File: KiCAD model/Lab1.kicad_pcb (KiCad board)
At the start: 2 copper layers, 60 x 40 mm, 47 parts, among them J1 USB_OTG, J2 SWD, SW2 Reset, U1 PMW3389, U2 AP2125N-3.3TRG, U3 MIC5235YM5-TR, U4 STM32F411RETx, U5 USBLC6-2SC6, Y1 16Mhz

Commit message: orgot the model
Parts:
- removed SW2: Reset, Button_Switch_SMD:SW_SPST_B3U-1000P
- added C22: 100n, Capacitor_SMD:C_0805_2012Metric_Pad1.18x1.45mm_HandSolder, F.Cu at (150.7, 85.9)
- added C23: 100n, Capacitor_SMD:C_0805_2012Metric_Pad1.18x1.45mm_HandSolder, F.Cu at (169.9, 67.1)
- added C24: 100n, Capacitor_SMD:C_0805_2012Metric_Pad1.18x1.45mm_HandSolder, F.Cu at (165.9, 71.7)
- added C25: 100n, Capacitor_SMD:C_0805_2012Metric_Pad1.18x1.45mm_HandSolder, F.Cu at (185.6, 52.3)
- added C26: 100n, Capacitor_SMD:C_0805_2012Metric_Pad1.18x1.45mm_HandSolder, F.Cu at (191.2, 48.9)
- added C27: 100n, Capacitor_SMD:C_0805_2012Metric_Pad1.18x1.45mm_HandSolder, F.Cu at (150.7, 88.9)
- added C28: 100n, Capacitor_SMD:C_0805_2012Metric_Pad1.18x1.45mm_HandSolder, F.Cu at (155.6, 84.2)
- added C30: 10u, Capacitor_SMD:C_0805_2012Metric_Pad1.18x1.45mm_HandSolder, F.Cu at (170.9, 73.2)
- added C31: 100n, Capacitor_SMD:C_0805_2012Metric_Pad1.18x1.45mm_HandSolder, F.Cu at (181.7, 60.1)
- added C32: 4.7u, Capacitor_SMD:C_0805_2012Metric_Pad1.18x1.45mm_HandSolder, F.Cu at (179.5, 66.4)
- added C33: 100n, Capacitor_SMD:C_0805_2012Metric_Pad1.18x1.45mm_HandSolder, F.Cu at (191.3, 55.3)
- added C34: 100n, Capacitor_SMD:C_0805_2012Metric_Pad1.18x1.45mm_HandSolder, F.Cu at (175.5, 70.2)
- added D4: Indicator LED, LED_SMD:LED_1206_3216Metric, F.Cu at (160.7, 71.8)
- added D5: Indicator LED, LED_SMD:LED_1206_3216Metric, F.Cu at (145.5, 86.1)
- added D6: Indicator LED, LED_SMD:LED_1206_3216Metric, F.Cu at (170.3, 63.9)
- added JP2: DFU, Connector:FanPinHeader_1x03_P2.54mm_Vertical, F.Cu at (185.4, 43.1)
- added JP3: DFU, Connector:FanPinHeader_1x03_P2.54mm_Vertical, F.Cu at (145.8, 80.0)
- added JP4: DFU, Connector:FanPinHeader_1x03_P2.54mm_Vertical, F.Cu at (171.9, 57.5)
- added R10: 10k, Resistor_SMD:R_0805_2012Metric_Pad1.20x1.40mm_HandSolder, F.Cu at (175.6, 76.1)
- added R11: 150, Resistor_SMD:R_0805_2012Metric_Pad1.20x1.40mm_HandSolder, F.Cu at (180.3, 69.3)
- added R12: 150, Resistor_SMD:R_0805_2012Metric_Pad1.20x1.40mm_HandSolder, F.Cu at (196.1, 53.4)
- added R13: 10k, Resistor_SMD:R_0805_2012Metric_Pad1.20x1.40mm_HandSolder, F.Cu at (170.9, 79.1)
- added R14: 10k, Resistor_SMD:R_0805_2012Metric_Pad1.20x1.40mm_HandSolder, F.Cu at (191.2, 64.2)
- added R15: 150, Resistor_SMD:R_0805_2012Metric_Pad1.20x1.40mm_HandSolder, F.Cu at (175.7, 73.1)
- added R16: 150, Resistor_SMD:R_0805_2012Metric_Pad1.20x1.40mm_HandSolder, F.Cu at (191.3, 58.3)
- added R17: 10k, Resistor_SMD:R_0805_2012Metric_Pad1.20x1.40mm_HandSolder, F.Cu at (205.6, 44.0)
- added R18: 10k, Resistor_SMD:R_0805_2012Metric_Pad1.20x1.40mm_HandSolder, F.Cu at (186.5, 64.2)
- added R19: 10k, Resistor_SMD:R_0805_2012Metric_Pad1.20x1.40mm_HandSolder, F.Cu at (200.8, 49.9)
- added R20: 10k, Resistor_SMD:R_0805_2012Metric_Pad1.20x1.40mm_HandSolder, F.Cu at (205.5, 47.0)
- added R21: 150, Resistor_SMD:R_0805_2012Metric_Pad1.20x1.40mm_HandSolder, F.Cu at (196.1, 59.3)
- added R22: 10k, Resistor_SMD:R_0805_2012Metric_Pad1.20x1.40mm_HandSolder, F.Cu at (200.9, 52.9)
- added R24: 820, Resistor_SMD:R_0805_2012Metric_Pad1.20x1.40mm_HandSolder, F.Cu at (180.4, 72.3)
- added R25: 820, Resistor_SMD:R_0805_2012Metric_Pad1.20x1.40mm_HandSolder, F.Cu at (185.0, 67.2)
- added R26: 820, Resistor_SMD:R_0805_2012Metric_Pad1.20x1.40mm_HandSolder, F.Cu at (170.0, 84.0)
- added R27: 47, Resistor_SMD:R_0805_2012Metric_Pad1.20x1.40mm_HandSolder, F.Cu at (191.2, 61.3)
- added R28: 10k, Resistor_SMD:R_0805_2012Metric_Pad1.20x1.40mm_HandSolder, F.Cu at (196.1, 56.3)
- added R7: 150, Resistor_SMD:R_0805_2012Metric_Pad1.20x1.40mm_HandSolder, F.Cu at (165.3, 84.0)
- added R8: 150, Resistor_SMD:R_0805_2012Metric_Pad1.20x1.40mm_HandSolder, F.Cu at (126.6, 89.0)
- added R9: 10k, Resistor_SMD:R_0805_2012Metric_Pad1.20x1.40mm_HandSolder, F.Cu at (165.0, 87.1)
- added S1: D2F-FL, Desktop:SW_D2F-FL, F.Cu at (37.0, 34.0)
- added S2: D2F-FL, Desktop:SW_D2F-FL, F.Cu at (72.9, 34.0)
- added S3: D2F-FL, Desktop:SW_D2F-FL, F.Cu at (62.0, 57.0)
- added S4: D2F-FL, Desktop:SW_D2F-FL, F.Cu at (48.0, 57.0)
- added S5: D2F-FL, Desktop:SW_D2F-FL, F.Cu at (34.3, 64.9)
- added S6: D2F-FL, Desktop:SW_D2F-FL, F.Cu at (34.3, 79.0)
- added S7: D2F-FL, Desktop:SW_D2F-FL, F.Cu at (71.0, 46.0)
- added SW1: 1825910-6, Desktop:SW_1825910-6-4, F.Cu at (125.0, 39.0)
- added SW10: Rotary_Encoder, Custom:PEC12R-2120F-N0012, F.Cu at (39.0, 57.0)
- added TP10: TestPoint, TestPoint:TestPoint_Pad_1.5x1.5mm, F.Cu at (179.8, 79.9)
- added TP11: TestPoint, TestPoint:TestPoint_Pad_1.5x1.5mm, F.Cu at (200.2, 59.7)
- added TP12: TestPoint, TestPoint:TestPoint_Pad_1.5x1.5mm, F.Cu at (172.7, 87.3)
- added TP13: TestPoint, TestPoint:TestPoint_Pad_1.5x1.5mm, F.Cu at (188.1, 71.0)
- added TP14: Scroll_b, TestPoint:TestPoint_Pad_1.5x1.5mm, F.Cu at (192.7, 67.5)
- added TP16: wheel_click, TestPoint:TestPoint_Pad_1.5x1.5mm, F.Cu at (183.3, 77.5)
- added TP17: in_D+, TestPoint:TestPoint_Pad_1.5x1.5mm, F.Cu at (203.8, 57.3)
- added TP18: Motion, TestPoint:TestPoint_Pad_1.5x1.5mm, F.Cu at (177.7, 83.5)
- added TP19: VDD, TestPoint:TestPoint_Pad_1.5x1.5mm, F.Cu at (184.6, 70.4)
- added TP20: NCS, TestPoint:TestPoint_Pad_1.5x1.5mm, F.Cu at (188.1, 74.6)
- added TP21: GND, TestPoint:TestPoint_Pad_1.5x1.5mm, F.Cu at (198.9, 63.2)
- added TP22: out_D-, TestPoint:TestPoint_Pad_1.5x1.5mm, F.Cu at (191.7, 71.0)
- added TP23: out_D+, TestPoint:TestPoint_Pad_1.5x1.5mm, F.Cu at (176.3, 87.0)
- added TP24: MISO, TestPoint:TestPoint_Pad_1.5x1.5mm, F.Cu at (196.3, 66.8)
- added TP25: GRD, TestPoint:TestPoint_Pad_1.5x1.5mm, F.Cu at (183.3, 81.1)
- added TP26: MCO1, TestPoint:TestPoint_Pad_1.5x1.5mm, F.Cu at (203.8, 60.9)
- added TP27: MCO2, TestPoint:TestPoint_Pad_1.5x1.5mm, F.Cu at (207.4, 57.3)
- added TP28: GND, TestPoint:TestPoint_Pad_1.5x1.5mm, F.Cu at (191.7, 74.6)
- added TP29: Scroll_a, TestPoint:TestPoint_Pad_1.5x1.5mm, F.Cu at (195.2, 71.0)
- added TP30: BOOT0, TestPoint:TestPoint_Pad_1.5x1.5mm, F.Cu at (186.9, 78.1)
- added TP5: TestPoint, TestPoint:TestPoint_Pad_1.5x1.5mm, F.Cu at (195.4, 62.5)
- added TP9: TestPoint, TestPoint:TestPoint_Pad_1.5x1.5mm, F.Cu at (205.0, 53.8)
- R1: value 1.5k -> 47; footprint Resistor_SMD:R_0815_2038Metric_Pad1.20x4.05mm_HandSolder -> Resistor_SMD:R_0805_2012Metric_Pad1.20x1.40mm_HandSolder
- R2, R3, R4, R5: footprint Resistor_SMD:R_0815_2038Metric_Pad1.20x4.05mm_HandSolder -> Resistor_SMD:R_0805_2012Metric_Pad1.20x1.40mm_HandSolder
- R6: value 47 -> 1.5k; footprint Resistor_SMD:R_0815_2038Metric_Pad1.20x4.05mm_HandSolder -> Resistor_SMD:R_0805_2012Metric_Pad1.20x1.40mm_HandSolder
- TP1: value TestPoint -> 5V
- TP2: value 1.9V -> MOSI
- TP3: value TestPoint -> SCK
- TP6: value TestPoint -> 3.3V
- TP7: value TestPoint -> NRST
- TP8: value TestPoint -> in_D-
- U1: footprint Battery:PMW3389 -> Custom:PMW3389
- moved C3 147.4 mm to (205.7, 41.0), turned to 0 degrees
- moved C4 147.2 mm to (200.9, 44.0)
- moved TP2 146.1 mm to (200.3, 56.1)
- moved C20 132.2 mm to (195.2, 44.4), turned to 0 degrees
- moved R6 131.7 mm to (186.5, 61.3), turned to 0 degrees
- moved TP6 131.5 mm to (205.0, 50.2)
- moved U3 130.7 mm to (181.7, 56.3), turned to 0 degrees
- moved C18 130.6 mm to (200.9, 41.0)
- moved R5 130.4 mm to (200.8, 47.0), turned to 0 degrees
- moved C2 129.5 mm to (196.0, 50.4), turned to 0 degrees
- moved D3 127.5 mm to (186.0, 49.1)
- moved R1 127.1 mm to (175.6, 79.1), turned to 0 degrees
- moved D2 126.7 mm to (195.6, 41.2)
- moved R3 124.2 mm to (170.9, 76.1), turned to 0 degrees
- moved C16 120.2 mm to (174.7, 67.1)
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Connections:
- R1 pad 1: Net-(D1-Pad2) -> Net-(JP2-Pad1)
- R1 pad 2: +5V -> Net-(D3-Pad2)
- R5 pad 1: Net-(D2-Pad2) -> Net-(JP3-Pad1)
- R5 pad 2: +3V3 -> Net-(D2-Pad2)
- R6 pad 1: Net-(D3-Pad2) -> Net-(JP4-Pad1)
- R6 pad 2: VDD -> Net-(D1-Pad2)
- TP1 pad 1: +3V3 -> +5V
- TP2 pad 1: VDD -> MOSI
- TP3 pad 1: Net-(C5-Pad2) -> SCK
- TP8 pad 1: BOOT0 -> IN_D-
- U4 pad 14: Net-(U4-Pad14) -> left_click
- U4 pad 15: Net-(U4-Pad15) -> right_click
- U4 pad 16: Net-(U4-Pad16) -> sense_up
- U4 pad 17: Net-(U4-Pad17) -> sense_down
- U4 pad 20: Net-(U4-Pad20) -> forward
- U4 pad 21: Net-(U4-Pad21) -> backward
- U4 pad 22: Net-(U4-Pad22) -> wheel_click
- U4 pad 23: Net-(U4-Pad23) -> RED
- U4 pad 26: Net-(U4-Pad26) -> MCO1
- U4 pad 27: Net-(U4-Pad27) -> MCO2
- U4 pad 41: Net-(U4-Pad41) -> GREEN
- U4 pad 42: Net-(U4-Pad42) -> BLUE
- U4 pad 43: Net-(U4-Pad43) -> OUT_D-
- U4 pad 44: OUT_D- -> OUT_D+
- U4 pad 45: OUT_D+ -> SWDIO
- U4 pad 46: SWDIO -> SWCLK
- U4 pad 49: SWCLK -> Scroll_a
- U4 pad 50: Net-(U4-Pad50) -> Scroll_b
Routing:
- net GND: track 297.8 -> 0.00 mm, vias 18 -> 0
- net +3V3: track 185.2 -> 0.00 mm, vias 8 -> 0
- net BOOT0: track 68.0 -> 0.00 mm, vias 5 -> 0
- net +5V: track 47.7 -> 0.00 mm
- net MISO: track 43.9 -> 0.00 mm
- net MOSI: track 41.2 -> 0.00 mm
- net OUT_D-: track 39.5 -> 0.00 mm, vias 2 -> 0
- net OUT_D+: track 38.6 -> 0.00 mm, vias 2 -> 0
- net VDD: track 35.8 -> 0.00 mm, vias 2 -> 0
- net NRST: track 35.5 -> 0.00 mm, vias 2 -> 0
- net Net-(C6-Pad2): track 31.3 -> 0.00 mm
- net Net-(C5-Pad2): track 27.3 -> 0.00 mm
- net SCK: track 23.2 -> 0.00 mm, vias 2 -> 0
- net Motion: track 19.2 -> 0.00 mm, vias 2 -> 0
- net NCS: track 16.5 -> 0.00 mm, vias 2 -> 0
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- removed copper zone on B.Cu, net GND
- removed copper zone on F.Cu, net GND
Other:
- board size 60 x 40 mm -> 50 x 80 mm

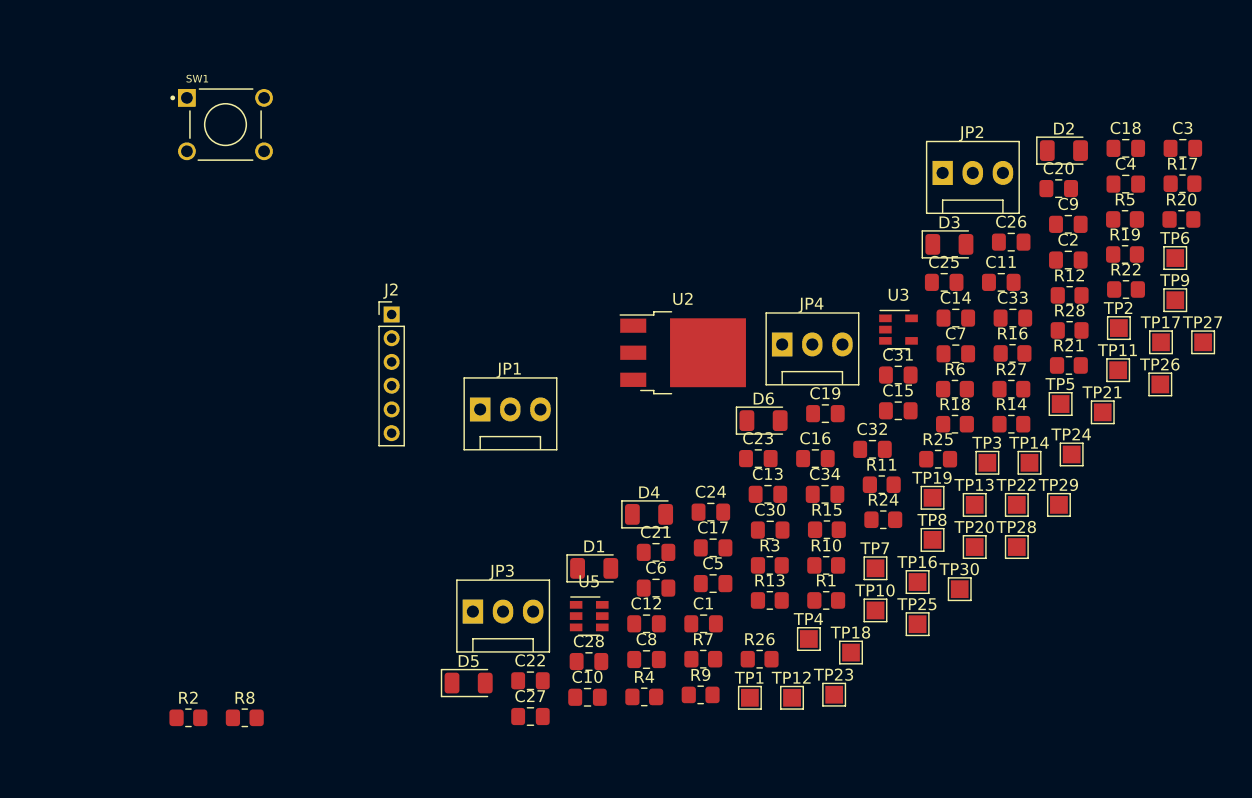
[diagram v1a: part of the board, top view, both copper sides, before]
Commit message: Fixed footprint for testpoints
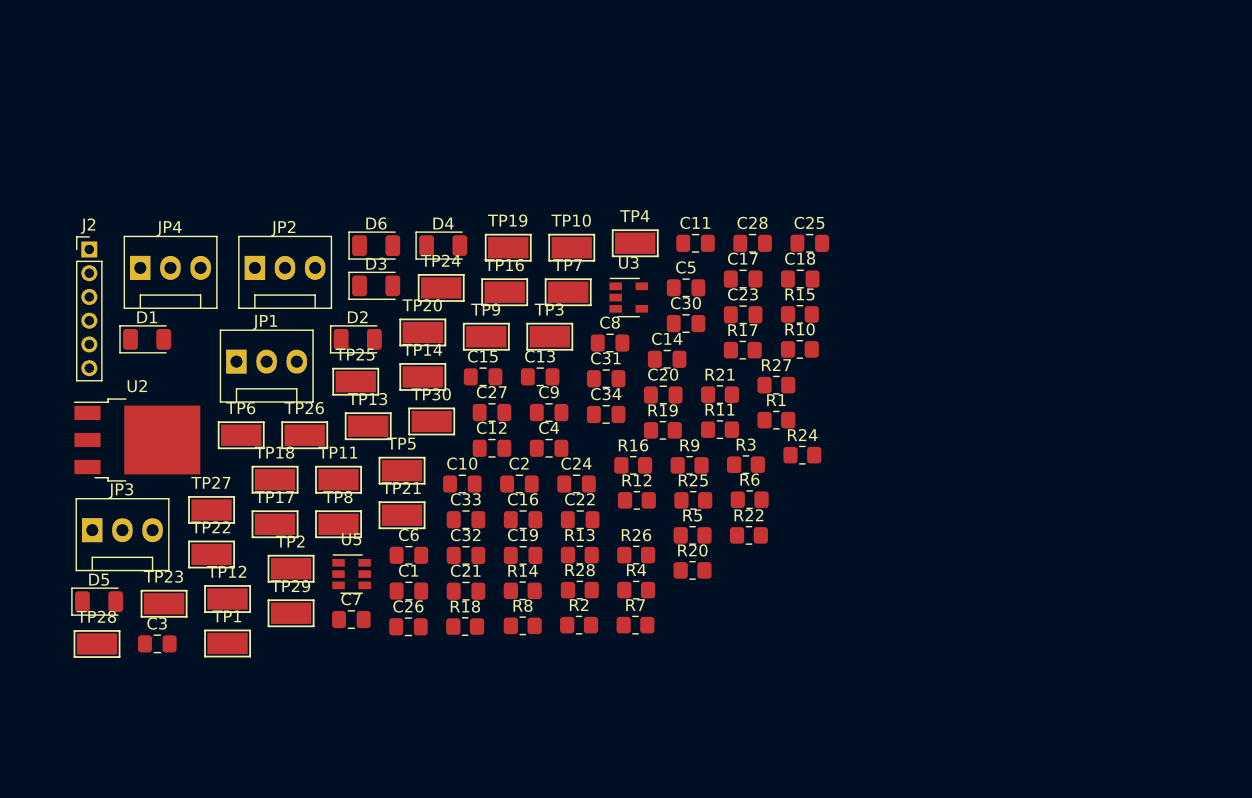
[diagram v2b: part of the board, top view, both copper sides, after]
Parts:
- removed SW1: 1825910-6, Desktop:SW_1825910-6-4
- TP1, TP10, TP11, TP12, TP13, TP14, TP16, TP17, TP18, TP19, TP2, TP20, TP21, TP22, TP23, TP24, TP25, TP26, TP27, TP28, TP29, TP3, TP30, TP4, TP5, TP6, TP7, TP8, TP9: footprint TestPoint:TestPoint_Pad_1.5x1.5mm -> TestPoint:TestPoint_Keystone_5015_Micro-Minature
- moved C3 96.0 mm to (119.3, 82.8)
- moved TP27 84.7 mm to (123.8, 71.5)
- moved TP6 80.1 mm to (126.3, 65.2)
- moved TP28 77.9 mm to (114.2, 82.8)
- moved TP17 76.2 mm to (129.2, 72.7)
- moved TP2 72.6 mm to (130.5, 76.4)
- moved TP26 72.2 mm to (131.7, 65.2)
- moved TP22 68.0 mm to (123.8, 75.2)
- moved TP11 66.3 mm to (134.5, 68.9)
- moved TP29 65.3 mm to (130.5, 80.2)
- moved D2 61.6 mm to (136.1, 57.1)
- moved C26 60.2 mm to (140.4, 81.3)
- moved TP21 59.7 mm to (139.9, 71.9)
- moved JP2 58.5 mm to (127.5, 51.1)
- moved TP9 58.1 mm to (147.0, 56.9)
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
